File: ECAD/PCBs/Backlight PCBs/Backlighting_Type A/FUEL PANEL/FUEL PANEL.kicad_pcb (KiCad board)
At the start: 2 copper layers, 128.6 x 74.2 mm, 65 parts, among them J1 Conn_01x04_Female, J2 Conn_01x04_Female

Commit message: Drawing Sheet & Silkscreen update - Backlight Panels (Fc thru Spin)
1:  Updated/Relinked Drawing Sheet for both PCB and Schematics
2:  Standardized Silkscreen (if required)

Finished Remaining Backlighting Type A & Type B PCBs.....
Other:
- board text added: "FUEL PANEL Revision: 3 www.openhornet.com"
- board text removed: "Fuel Panel Backlight Designed by L. Walker"
- board text removed: "Version 2.2"
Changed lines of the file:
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@@
   )
   (paper "A4")
+  (title_block
+    (title "FUEL PANEL")
+    (date "2023-02-10")
+    (rev "3")
+  )
   (layers
     (0 "F.Cu" signal)
@@
     (effects (font (size 1 1) (thickness 0.15)) (justify mirror))
   )
-  (gr_text "Version 2.2" (at 198.12 95.25) (layer "B.SilkS")
-    (effects (font (size 1 1) (thickness 0.15)) (justify mirror))
-  )
   (gr_text "Switch PCB\nH1" (at 179.8828 83.3628) (layer "B.SilkS")
     (effects (font (size 1 1) (thickness 0.15)) (justify mirror))
@@
     (effects (font (size 1 1) (thickness 0.15)) (justify mirror))
   )
-  (gr_text "Fuel Panel Backlight\nDesigned by L. Walker" (at 141.58468 141.84122) (layer "B.SilkS")
-    (effects (font (size 1 1) (thickness 0.15)) (justify left mirror))
+  (gr_text "FUEL PANEL\nRevision: 3\nwww.openhornet.com" (at 131.7498 136.1694) (layer "B.SilkS")
+    (effects (font (size 1 1) (thickness 0.15)) (justify mirror))
   )
   (gr_text "Molex 2X2 Mini-Fit Jr." (at 154.54884 125.65634) (layer "B.SilkS")

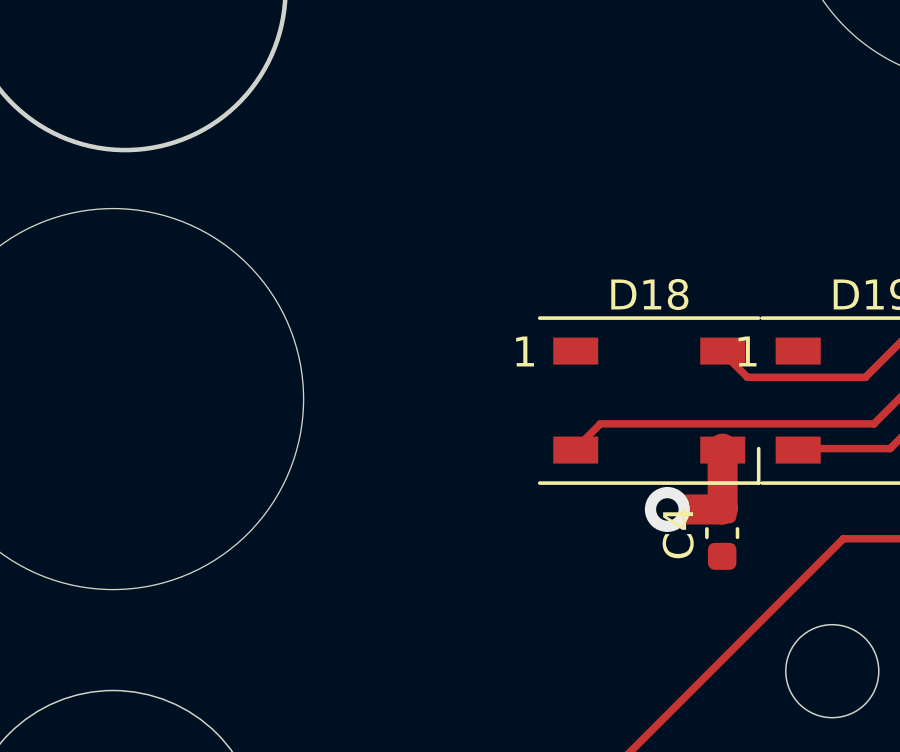
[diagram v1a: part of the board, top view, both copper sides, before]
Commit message: Review: FIRE TEST thru HUD 100%
Reviewed/adjusted silkscreens as needed
Relinked footprints
Updated Manufacturing files
Updated PNGs and STEP files as needed.
Renamed PNGs for standardization
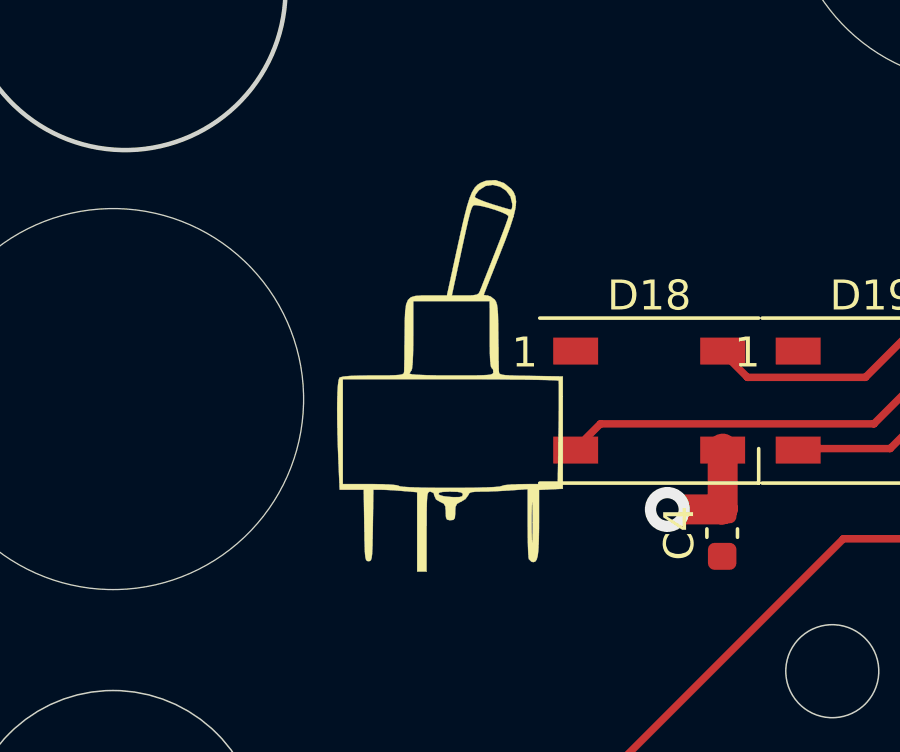
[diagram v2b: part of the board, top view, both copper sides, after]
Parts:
- 1, 2, 3: footprint OH_Backlighting:SxAL_Toggle_13x13mm -> OH_Footprints:SxAL_Toggle_13x13mm
- 5 (x2), 6: footprint OH_Backlighting:OH_Panel_6-32_PHS -> OH_Footprints:OH_Panel_6-32_PHS
- 7: footprint OH_Backlighting:631H_Toggle_13mm_x_13mm -> OH_Footprints:631H_Toggle_13mm_x_13mm
- G*** (x3): footprint Kicad Footprint Files:S3ALToggle -> OH_Footprints:S3ALToggle
- G***: footprint Kicad Footprint Files:631HToggle -> OH_Footprints:631H_Toggle_Silkscreen
- G***: footprint OH_General:CC-BY-NC-SA-Small -> OH_Footprints:CC-BY-NC-SA-Small
- G***: footprint OH_General:OH_LOGO_37.7mm_5.9mm -> OH_Footprints:OH_LOGO_37.7mm_5.9mm

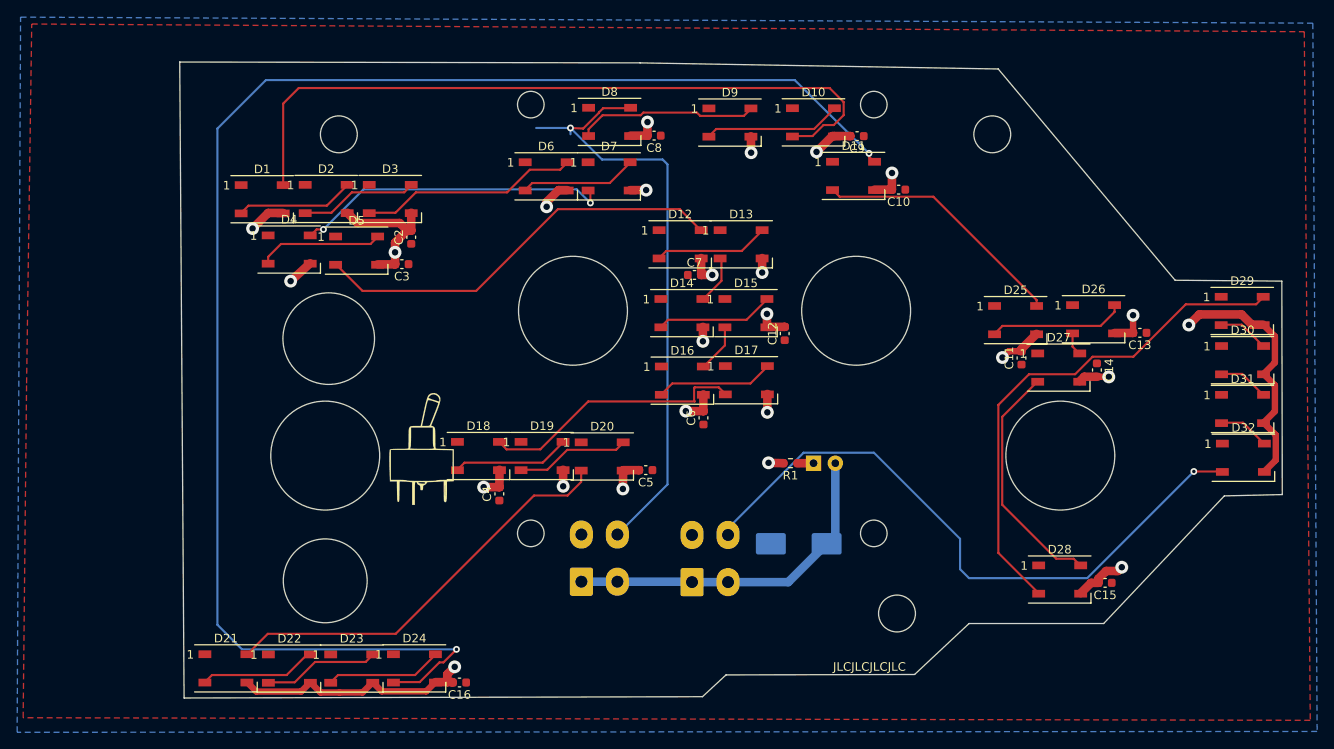
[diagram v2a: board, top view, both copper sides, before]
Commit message: KiCad 7 Transition - FUEL Panel
Footprints- Updated metadata for Switch Silkscreens
FCS Panel - Fixed position of legend boxes

FUEL Panel
-Schematic and PCB Standardization
-Updated value for MAG Switch, specifically
-Fixed traces for DIN/DOUT
-Additional minor changes to traces for PWR plane conflicts
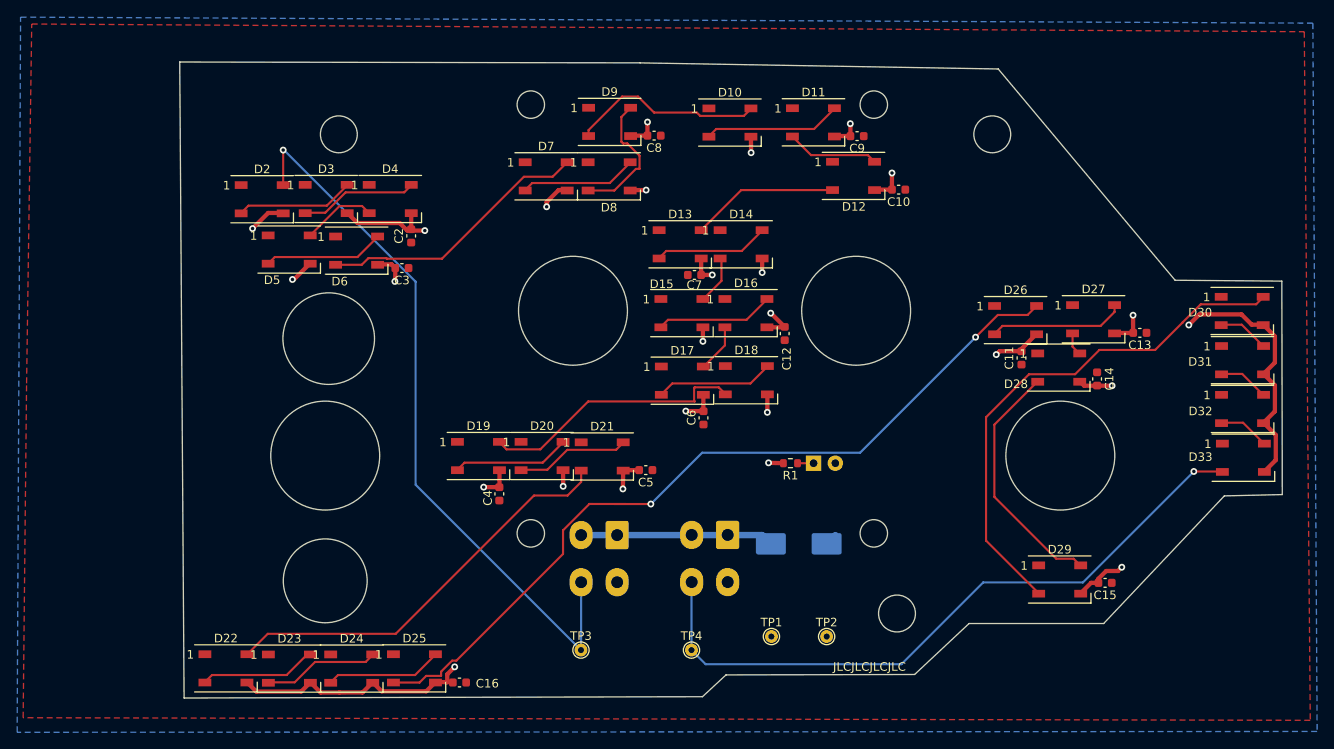
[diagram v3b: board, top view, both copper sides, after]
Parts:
- removed 1, 2, 3: SxAL_Toggle_13x13mm, OH_Footprints:SxAL_Toggle_13x13mm
- removed 5 (x2), 6: OH_Panel_Fastner_Keepout, OH_Footprints:OH_Panel_6-32_PHS
- removed 7: 631H_Toggle_13mm_x_13mm, OH_Footprints:631H_Toggle_13mm_x_13mm
- added MH1: 6x32 / 4mm, OH_Footprints:MountingHole_6-32_PHS, B.Cu at (117.6, 83.5)
- added MH10: Switch_NKK SxAL, OH_Footprints:SxAL_Toggle_13x13mm, F.Cu at (144.9, 104.0)
- added MH11: Switch_NKK SxAL, OH_Footprints:SxAL_Toggle_13x13mm, F.Cu at (177.9, 104.0)
- added MH12: Switch_631H, OH_Footprints:631HX_Toggle_13mm_x_13mm, F.Cu at (201.8, 120.9)
- added MH2: 6x32 / 4mm, OH_Footprints:MountingHole_6-32_PHS, B.Cu at (193.8, 83.5)
- added MH3: 6x32 / 4mm, OH_Footprints:MountingHole_6-32_PHS, B.Cu at (182.7, 139.3)
- added MH5: M3 / 3.2mm, OH_Footprints:MountingHole_3.2mm_M3_DIN965, B.Cu at (140.0, 80.0)
- added MH6: M3 / 3.2mm, OH_Footprints:MountingHole_3.2mm_M3_DIN965, B.Cu at (180.0, 80.0)
- added MH7: M3 / 3.2mm, OH_Footprints:MountingHole_3.2mm_M3_DIN965, B.Cu at (140.0, 130.0)
- added MH8: M3 / 3.2mm, OH_Footprints:MountingHole_3.2mm_M3_DIN965, B.Cu at (180.0, 130.0)
- added MH9: Switch_631H, OH_Footprints:631HX_Toggle_13mm_x_13mm, F.Cu at (116.0, 120.9)
- added TP1: TestPoint, OH_Footprints:TestPoint_THTPad_D1.5mm_Drill0.7mm, F.Cu at (168.1, 142.0)
- added TP2: TestPoint, OH_Footprints:TestPoint_THTPad_D1.5mm_Drill0.7mm, F.Cu at (174.5, 142.0)
- added TP3: TestPoint, OH_Footprints:TestPoint_THTPad_D1.5mm_Drill0.7mm, F.Cu at (145.8, 143.6)
- added TP4: TestPoint, OH_Footprints:TestPoint_THTPad_D1.5mm_Drill0.7mm, F.Cu at (158.7, 143.6)
- C1: value C_Polarized -> 1000uF
- C10, C11, C12, C13, C14, C15, C16, C2, C3, C4, C5, C6, C7, C8, C9: value C -> 0.1uF
- D1: renamed from D33; value LED -> Green
- J1, J2: value Conn_01x04_Female -> Mini-Fit Jr. 2x02
- LOGO1: renamed from G***; footprint OH_Footprints:OH_LOGO_37.7mm_5.9mm -> OH_Footprints:LOGO_OH_Text_Small
- LOGO2: renamed from G***; footprint OH_Footprints:CC-BY-NC-SA-Small -> OH_Footprints:LOGO_CC-BY-NC-SA_Half_Small
- LOGO3: renamed from G***; footprint OH_Footprints:631H_Toggle_Silkscreen -> OH_Footprints:631H3_Toggle_Silkscreen
- LOGO4, LOGO5: renamed from G***; footprint OH_Footprints:S3ALToggle -> OH_Footprints:S3AL_Toggle_Silkscreen
- LOGO6: renamed from G***; footprint OH_Footprints:S3ALToggle -> OH_Footprints:631H2_Toggle_Silkscreen
- R1: value R -> 470
- moved LOGO2 50.0 mm to (127.3, 144.9)
- moved LOGO1 17.0 mm to (161.1, 90.8)
- moved J2 6.90 mm to (163.0, 130.2), turned to 180 degrees
- moved J1 6.85 mm to (150.1, 130.2), turned to 180 degrees
- moved LOGO6 1.50 mm to (212.8, 119.6)
- moved C14 1.04 mm to (206.0, 112.0)
- moved C3 0.45 mm to (125.0, 99.1)
- moved C2 0.15 mm to (126.0, 95.3)
- turned C1 to 0 degrees
- renumbered D9 to D10, D10 to D11, D11 to D12, D12 to D13, D13 to D14, D14 to D15, D15 to D16, D16 to D17, D17 to D18, D18 to D19, D1 to D2, D19 to D20, D20 to D21, D21 to D22, D22 to D23, D23 to D24, D24 to D25, D25 to D26, D26 to D27, D27 to D28, D28 to D29, D2 to D3, D29 to D30, D30 to D31, D31 to D32, D32 to D33, D3 to D4, D4 to D5, D5 to D6, D6 to D7, D7 to D8, D8 to D9
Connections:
- net /DATAOUT renamed DATA OUT
- net /LED+5V renamed +5V
- net /LEDGND renamed GND
- net Net-(D16-Pad2) renamed /DATA2
- net Net-(D8-Pad2) renamed /DATA1
- D11 pad 2: Net-(D1-Pad4) -> Net-(D11-DOUT)
- D12 pad 2: Net-(D11-Pad2) -> Net-(D12-DOUT)
- D12 pad 4: Net-(D11-Pad4) -> Net-(D11-DOUT)
- D13 pad 4: Net-(D12-Pad4) -> Net-(D12-DOUT)
- D2 pad 4: Net-(D1-Pad4) -> DATA IN
- D25 pad 2: Net-(D11-Pad4) -> /DATA3
- D26 pad 4: Net-(D11-Pad2) -> /DATA3
- D4 pad 2: Net-(D3-Pad2) -> Net-(D4-DOUT)
- D5 pad 4: Net-(D4-Pad4) -> Net-(D4-DOUT)
- D6 pad 2: Net-(D12-Pad4) -> Net-(D6-DOUT)
- D7 pad 4: Net-(D3-Pad2) -> Net-(D6-DOUT)
- D8 pad 2: Net-(D4-Pad4) -> Net-(D8-DOUT)
- D9 pad 4: /DATAIN -> Net-(D8-DOUT)
- J1 pad 4: /DATAIN -> DATA IN
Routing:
- net Net-(D11-Pad4): track 179.1 -> 0.00 mm, vias 2 -> 0
- net /DATA3: track 0.00 -> 95.1 mm, vias 0 -> 2
- net Net-(D1-Pad4): track 84.9 -> 0.00 mm
- net DATA IN: track 0.00 -> 84.7 mm, vias 0 -> 1
- net /DATAIN: track 71.5 -> 0.00 mm, vias 1 -> 0
- net Net-(D12-Pad4): track 48.9 -> 0.00 mm
- net Net-(D4-Pad4): track 37.2 -> 0.00 mm, vias 2 -> 0
- net Net-(D6-DOUT): track 0.00 -> 32.0 mm
- net Net-(D11-Pad2): track 29.9 -> 0.00 mm
- net Net-(D3-Pad2): track 25.5 -> 0.00 mm
- net +5V: track 40.3 -> 22.5 mm
- net Net-(D12-DOUT): track 0.00 -> 17.3 mm
- net Net-(D8-DOUT): track 0.00 -> 15.8 mm
- net Net-(D11-DOUT): track 0.00 -> 10.8 mm
- net Net-(D4-DOUT): track 0.00 -> 8.65 mm
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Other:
- outline, holes or cut-outs redrawn
- board text added: "FINGER GUARD NUTS SECURE TO THE BACKPLATE. NOT THIS PCB"
- board text added: "FUEL PANEL REV: 4 WWW.OPENHORNET.COM"
- board text removed: "3"
- board text removed: "FINGER GUARD NUTS SECURE TO THE BACKPLATE NOT THIS PCB"
- board text removed: "FUEL PANEL Revision: 3 www.openhornet.com"
- board text removed: "IN"
- board text removed: "Switch PCB H1"
- board text removed: "Switch PCB H2"
- board text removed: "Switch PCB H3"
- board text removed: "Switch PCB H4"
- board text removed: "THRU"
- board text removed: "⌀3MM"
